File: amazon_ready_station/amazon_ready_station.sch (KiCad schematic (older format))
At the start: 25 parts, among them J1 ESP 32 Left VIN GND to VP EN, J2 IR_RECVR_GND_VIN_DAT, J5 ESP32 Right 3V3 GND to D22 D23, J7 BRKOUT_LEFT, J8 BRKOUT_RIGHT, Q1 2N2219

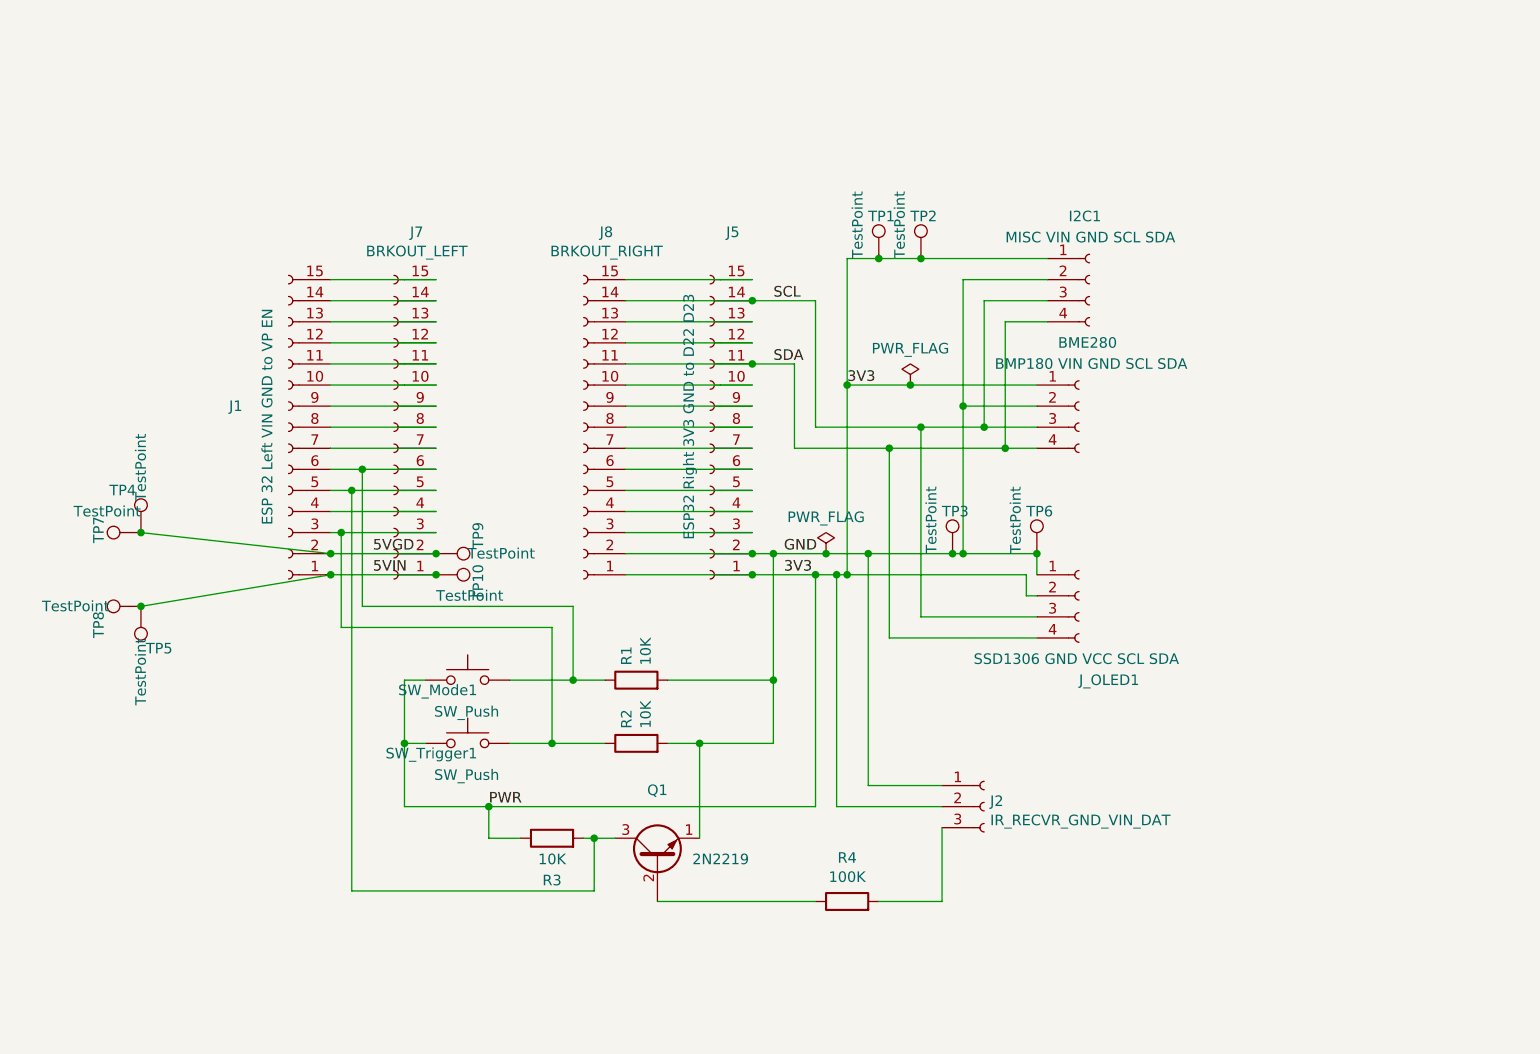
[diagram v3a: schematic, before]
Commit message: added screw holes and edited Pwr In plates
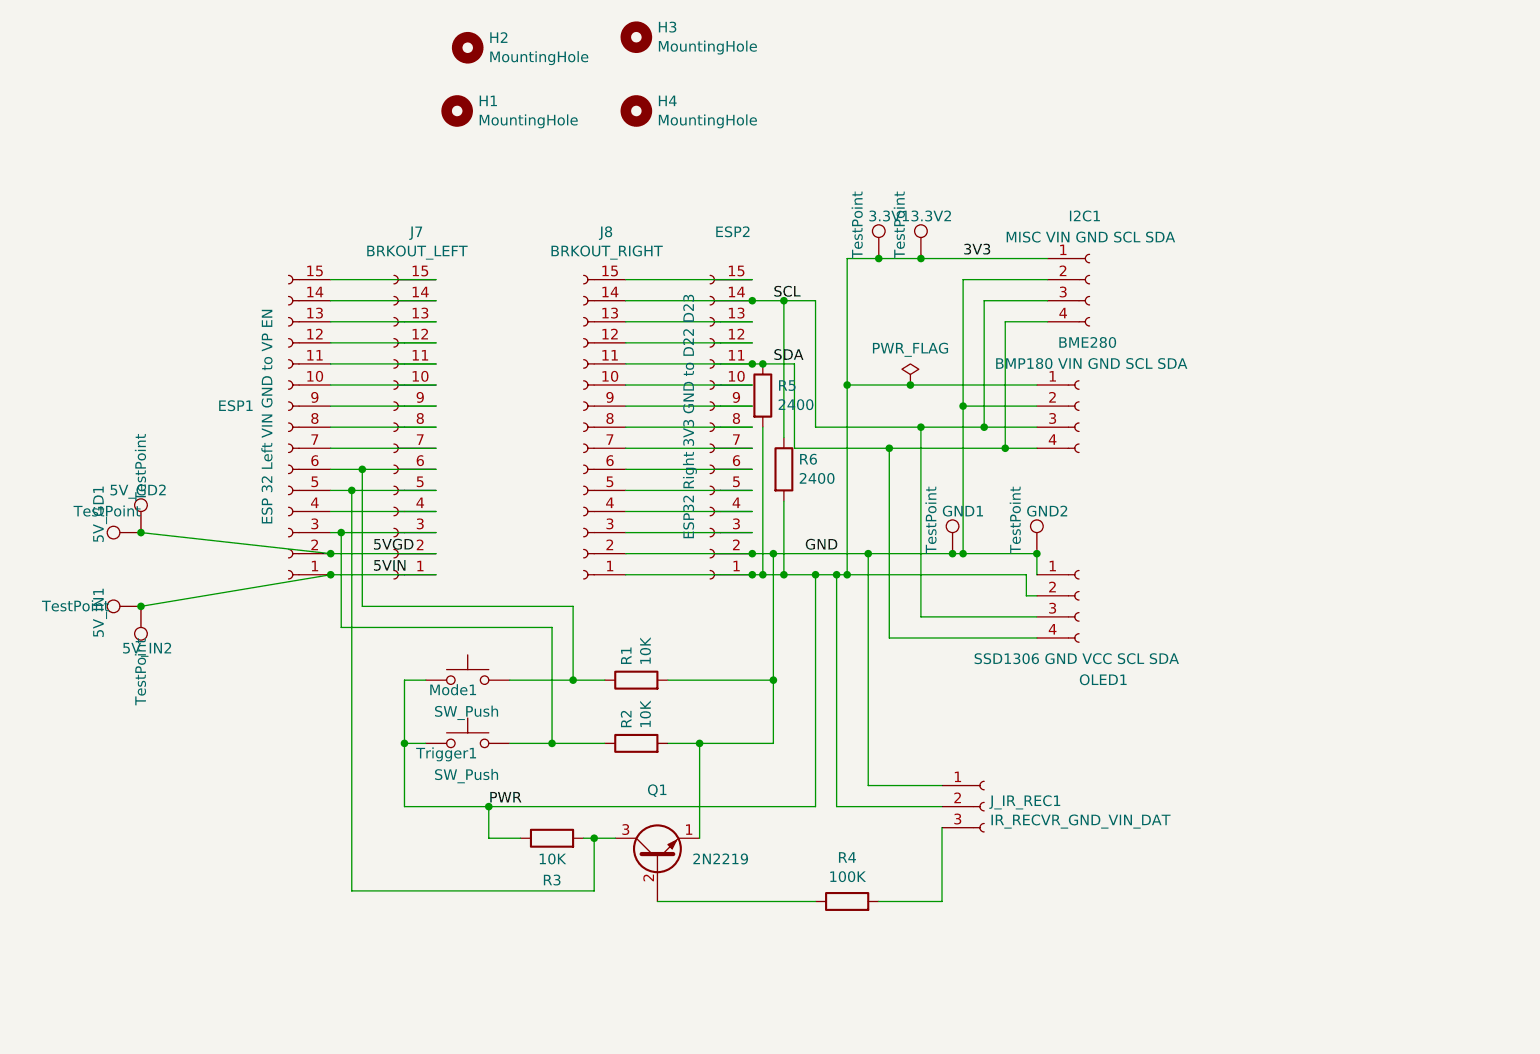
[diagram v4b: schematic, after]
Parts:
- removed TP10: TestPoint, amazon_ready_station:pad_left, symbol Connector:TestPoint
- removed TP9: TestPoint, amazon_ready_station:pad_right, symbol Connector:TestPoint
- added H1, H2, H3, H4: MountingHole, MountingHole:MountingHole_2.2mm_M2, symbol Mechanical:MountingHole
- added R5, R6: 2400, Resistor_SMD:R_0805_2012Metric_Pad1.20x1.40mm_HandSolder, symbol Device:R
- renumbered TP1 to 3.3V1, TP2 to 3.3V2, TP7 to 5V_GD1, TP4 to 5V_GD2, TP8 to 5V_IN1, TP5 to 5V_IN2, J1 to ESP1, J5 to ESP2, TP3 to GND1, TP6 to GND2, J2 to J_IR_REC1, SW_Mode1 to Mode1, J_OLED1 to OLED1, SW_Trigger1 to Trigger1
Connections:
- net 3V3: now also R5.2, R6.2
- net SCL: now also R6.1
- net SDA: now also R5.1
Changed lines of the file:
@@
 $EndComp
 $Comp
-L power:PWR_FLAG #FLG02
-U 1 1 604AC76B
-P 4700 4750
-F 0 "#FLG02" H 4700 4825 50  0001 C CNN
-F 1 "PWR_FLAG" H 4700 4923 50  0000 C CNN
-F 2 "" H 4700 4750 50  0001 C CNN
-F 3 "~" H 4700 4750 50  0001 C CNN
-	1    4700 4750
-	1    0    0    -1
-$EndComp
-$Comp
-L Connector:Conn_01x15_Female J1
+L Connector:Conn_01x15_Female ESP1
 U 1 1 604B94AB
 P 2150 4150
-F 0 "J1" H 2400 4050 50  0000 C CNN
+F 0 "ESP1" H 2400 4050 50  0000 C CNN
 F 1 "ESP 32 Left VIN GND to VP EN" V 2250 4100 50  0000 C CNN
 F 2 "Connector_PinSocket_2.54mm:PinSocket_1x15_P2.54mm_Vertical" H 2150 4150 50  0001 C CNN
@@
 $EndComp
 Wire Wire Line
-	4350 3850 4550 3850
-Wire Wire Line
-	4350 3550 4650 3550
+	4350 3850 4400 3850
+Wire Wire Line
+	4350 3550 4500 3550
 $Comp
 L Connector:Conn_01x04_Female BME280
@@
 $EndComp
 $Comp
-L Connector:Conn_01x04_Female J_OLED1
+L Connector:Conn_01x04_Female OLED1
 U 1 1 604E4BCE
 P 5900 4950
-F 0 "J_OLED1" H 5900 4550 50  0000 L CNN
+F 0 "OLED1" H 5900 4550 50  0000 L CNN
 F 1 "SSD1306 GND VCC SCL SDA" H 5400 4650 50  0000 L CNN
 F 2 "Connector_PinSocket_2.54mm:PinSocket_1x04_P2.54mm_Vertical" H 5900 4950 50  0001 C CNN
@@
 $EndComp
 $Comp
-L Connector:Conn_01x15_Female J5
+L Connector:Conn_01x15_Female ESP2
 U 1 1 604EB918
 P 4150 4150
-F 0 "J5" H 4042 3225 50  0000 C CNN
+F 0 "ESP2" H 4042 3225 50  0000 C CNN
 F 1 "ESP32 Right 3V3 GND to D22 D23" V 4250 4100 50  0000 C CNN
 F 2 "Connector_PinSocket_2.54mm:PinSocket_1x15_P2.54mm_Vertical" H 4150 4150 50  0001 C CNN
@@
 	-1   0    0    1
 $EndComp
-Text Label 4500 4750 0    50   ~ 0
+Text Label 4600 4750 0    50   ~ 0
 GND
 Text Label 4450 3850 0    50   ~ 0
@@
 Text Label 4450 3550 0    50   ~ 0
 SCL
-Text Label 4500 4850 0    50   ~ 0
-3V3
 Connection ~ 4450 4750
-Wire Wire Line
-	4450 4750 4700 4750
 $Comp
 L Device:R R1
@@
 $EndComp
 $Comp
-L Switch:SW_Push SW_Trigger1
+L Switch:SW_Push Trigger1
 U 1 1 604FFFBF
 P 3000 5650
-F 0 "SW_Trigger1" H 3046 5602 50  0000 R CNN
+F 0 "Trigger1" H 3046 5602 50  0000 R CNN
 F 1 "SW_Push" H 3150 5500 50  0000 R CNN
 F 2 "Button_Switch_SMD:SW_Push_1P1T_NO_6x6mm_H9.5mm" H 3000 5850 50  0001 C CNN
@@
 	4650 6400 3900 6400
 $Comp
-L Connector:Conn_01x03_Female J2
+L Connector:Conn_01x03_Female J_IR_REC1
 U 1 1 60683231
 P 5450 5950
-F 0 "J2" H 5478 5976 50  0000 L CNN
+F 0 "J_IR_REC1" H 5478 5976 50  0000 L CNN
 F 1 "IR_RECVR_GND_VIN_DAT" H 5478 5885 50  0000 L CNN
 F 2 "Connector_PinSocket_2.54mm:PinSocket_1x03_P2.54mm_Horizontal" H 5450 5950 50  0001 C CNN
@@
 Wire Wire Line
 	5550 4250 5700 4250
-Text Label 4800 3950 0    50   ~ 0
-3V3
 Wire Wire Line
 	4800 3950 4800 4850
@@
 	4450 4750 4450 5350
 Wire Wire Line
-	4350 4850 4650 4850
+	4350 4850 4400 4850
 Wire Wire Line
 	4800 3350 4800 3950
@@
 Wire Wire Line
 	5000 4250 5550 4250
-Connection ~ 4700 4750
 Wire Wire Line
 	5150 4150 5150 5050
@@
 	5150 4150 5450 4150
 $Comp
-L Connector:TestPoint TP1
+L Connector:TestPoint 3.3V1
 U 1 1 607606D6
 P 4950 3350
-F 0 "TP1" H 4900 3550 50  0000 L CNN
+F 0 "3.3V1" H 4900 3550 50  0000 L CNN
 F 1 "TestPoint" V 4850 3350 50  0000 L CNN
 F 2 "TestPoint:TestPoint_THTPad_D2.0mm_Drill1.0mm" H 5150 3350 50  0001 C CNN
@@
 Connection ~ 4950 3350
 $Comp
-L Connector:TestPoint TP2
+L Connector:TestPoint 3.3V2
 U 1 1 6076206D
 P 5150 3350
-F 0 "TP2" H 5100 3550 50  0000 L CNN
+F 0 "3.3V2" H 5100 3550 50  0000 L CNN
 F 1 "TestPoint" V 5050 3350 50  0000 L CNN
 F 2 "TestPoint:TestPoint_THTPad_D2.0mm_Drill1.0mm" H 5350 3350 50  0001 C CNN
@@
 Connection ~ 5150 3350
 $Comp
-L Connector:TestPoint TP3
+L Connector:TestPoint GND1
 U 1 1 60762F17
 P 5300 4750
-F 0 "TP3" H 5250 4950 50  0000 L CNN
+F 0 "GND1" H 5250 4950 50  0000 L CNN
 F 1 "TestPoint" V 5200 4750 50  0000 L CNN
 F 2 "TestPoint:TestPoint_THTPad_D2.0mm_Drill1.0mm" H 5500 4750 50  0001 C CNN
@@
 	5300 4750 5350 4750
 $Comp
-L Connector:TestPoint TP6
+L Connector:TestPoint GND2
 U 1 1 6076314C
 P 5700 4750
-F 0 "TP6" H 5650 4950 50  0000 L CNN
+F 0 "GND2" H 5650 4950 50  0000 L CNN
 F 1 "TestPoint" V 5600 4750 50  0000 L CNN
 F 2 "TestPoint:TestPoint_THTPad_D2.0mm_Drill1.0mm" H 5900 4750 50  0001 C CNN
@@
 Text Label 2550 4750 0    50   ~ 0
 5VGD
-Connection ~ 2850 4850
-$Comp
-L Connector:TestPoint TP10
-U 1 1 605C250F
-P 2850 4850
-F 0 "TP10" H 2800 5050 50  0000 L CNN
-F 1 "TestPoint" V 2950 4850 50  0000 L CNN
-F 2 "amazon_ready_station:pad_left" H 3050 4850 50  0001 C CNN
-F 3 "~" H 3050 4850 50  0001 C CNN
-	1    2850 4850
-	0    1    1    0
-$EndComp
-$Comp
-L Connector:TestPoint TP9
-U 1 1 605C4012
-P 2850 4750
-F 0 "TP9" H 2700 4950 50  0000 L CNN
-F 1 "TestPoint" V 2850 4900 50  0000 L CNN
-F 2 "amazon_ready_station:pad_right" H 3050 4750 50  0001 C CNN
-F 3 "~" H 3050 4750 50  0001 C CNN
-	1    2850 4750
-	0    1    1    0
-$EndComp
-Connection ~ 2850 4750
 Wire Wire Line
 	2350 4750 1450 4650
@@
 Connection ~ 2350 4850
 $Comp
-L Connector:TestPoint TP8
+L Connector:TestPoint 5V_IN1
 U 1 1 605CDAFA
 P 1450 5000
-F 0 "TP8" H 1300 5200 50  0000 L CNN
+F 0 "5V_IN1" H 1300 5200 50  0000 L CNN
 F 1 "TestPoint" V 1450 5150 50  0000 L CNN
 F 2 "TestPoint:TestPoint_THTPad_D2.0mm_Drill1.0mm" H 1650 5000 50  0001 C CNN
@@
 $EndComp
 $Comp
-L Connector:TestPoint TP7
+L Connector:TestPoint 5V_GD1
 U 1 1 605CE0C4
 P 1450 4650
-F 0 "TP7" H 1400 4850 50  0000 L CNN
+F 0 "5V_GD1" H 1400 4850 50  0000 L CNN
 F 1 "TestPoint" V 1550 4650 50  0000 L CNN
 F 2 "TestPoint:TestPoint_THTPad_D2.0mm_Drill1.0mm" H 1650 4650 50  0001 C CNN
@@
 $EndComp
 Wire Wire Line
-	4700 4750 4900 4750
-Wire Wire Line
 	4900 4750 4900 5850
 Wire Wire Line
@@
 	5350 4750 5700 4750
 $Comp
-L Switch:SW_Push SW_Mode1
+L Switch:SW_Push Mode1
 U 1 1 6063A1F9
 P 3000 5350
-F 0 "SW_Mode1" H 3046 5302 50  0000 R CNN
+F 0 "Mode1" H 3046 5302 50  0000 R CNN
 F 1 "SW_Push" H 3150 5200 50  0000 R CNN
 F 2 "Button_Switch_SMD:SW_Push_1P1T_NO_6x6mm_H9.5mm" H 3000 5550 50  0001 C CNN
@@
 	2800 5350 2700 5350
 $Comp
-L Connector:TestPoint TP5
+L Connector:TestPoint 5V_IN2
 U 1 1 60657975
 P 1450 5000
-F 0 "TP5" H 1300 5200 50  0000 L CNN
+F 0 "5V_IN2" H 1300 5200 50  0000 L CNN
 F 1 "TestPoint" V 1450 5150 50  0000 L CNN
 F 2 "TestPoint:TestPoint_THTPad_D2.0mm_Drill1.0mm" H 1650 5000 50  0001 C CNN
@@
 Connection ~ 1450 5000
 $Comp
-L Connector:TestPoint TP4
+L Connector:TestPoint 5V_GD2
 U 1 1 60658198
 P 1450 4650
-F 0 "TP4" H 1300 4850 50  0000 L CNN
+F 0 "5V_GD2" H 1300 4850 50  0000 L CNN
 F 1 "TestPoint" V 1450 4800 50  0000 L CNN
 F 2 "TestPoint:TestPoint_THTPad_D2.0mm_Drill1.0mm" H 1650 4650 50  0001 C CNN
@@
 $EndComp
 Connection ~ 1450 4650
+$Comp
+L Device:R R5
+U 1 1 605D37E2
+P 4400 4000
+F 0 "R5" H 4470 4046 50  0000 L CNN
+F 1 "2400" H 4470 3955 50  0000 L CNN
+F 2 "Resistor_SMD:R_0805_2012Metric_Pad1.20x1.40mm_HandSolder" V 4330 4000 50  0001 C CNN
+F 3 "~" H 4400 4000 50  0001 C CNN
+	1    4400 4000
+	1    0    0    -1
+$EndComp
+Connection ~ 4400 3850
+Wire Wire Line
+	4400 3850 4550 3850
+Wire Wire Line
+	4400 4150 4400 4850
+Connection ~ 4400 4850
+Wire Wire Line
+	4400 4850 4500 4850
+$Comp
+L Device:R R6
+U 1 1 605D9489
+P 4500 4350
+F 0 "R6" H 4570 4396 50  0000 L CNN
+F 1 "2400" H 4570 4305 50  0000 L CNN
+F 2 "Resistor_SMD:R_0805_2012Metric_Pad1.20x1.40mm_HandSolder" V 4430 4350 50  0001 C CNN
+F 3 "~" H 4500 4350 50  0001 C CNN
+	1    4500 4350
+	1    0    0    -1
+$EndComp
+Wire Wire Line
+	4500 3550 4500 4200
+Connection ~ 4500 3550
+Wire Wire Line
+	4500 3550 4650 3550
+Connection ~ 4500 4850
+Wire Wire Line
+	4500 4850 4650 4850
+Wire Wire Line
+	4500 4500 4500 4850
+$Comp
+L Mechanical:MountingHole H2
+U 1 1 6062E33E
+P 3000 2350
+F 0 "H2" H 3100 2396 50  0000 L CNN
+F 1 "MountingHole" H 3100 2305 50  0000 L CNN
+F 2 "MountingHole:MountingHole_2.2mm_M2" H 3000 2350 50  0001 C CNN
+F 3 "~" H 3000 2350 50  0001 C CNN
+	1    3000 2350
+	1    0    0    -1
+$EndComp
+$Comp
+L Mechanical:MountingHole H3
+U 1 1 6062E7A6
+P 3800 2300
+F 0 "H3" H 3900 2346 50  0000 L CNN
+F 1 "MountingHole" H 3900 2255 50  0000 L CNN
+F 2 "MountingHole:MountingHole_2.2mm_M2" H 3800 2300 50  0001 C CNN
+F 3 "~" H 3800 2300 50  0001 C CNN
+	1    3800 2300
+	1    0    0    -1
+$EndComp
+$Comp
+L Mechanical:MountingHole H4
+U 1 1 6062E97D
+P 3800 2650
+F 0 "H4" H 3900 2696 50  0000 L CNN
+F 1 "MountingHole" H 3900 2605 50  0000 L CNN
+F 2 "MountingHole:MountingHole_2.2mm_M2" H 3800 2650 50  0001 C CNN
+F 3 "~" H 3800 2650 50  0001 C CNN
+	1    3800 2650
+	1    0    0    -1
+$EndComp
+$Comp
+L Mechanical:MountingHole H1
+U 1 1 6062EB1C
+P 2950 2650
+F 0 "H1" H 3050 2696 50  0000 L CNN
+F 1 "MountingHole" H 3050 2605 50  0000 L CNN
+F 2 "MountingHole:MountingHole_2.2mm_M2" H 2950 2650 50  0001 C CNN
+F 3 "~" H 2950 2650 50  0001 C CNN
+	1    2950 2650
+	1    0    0    -1
+$EndComp
+Wire Wire Line
+	4450 4750 4900 4750
+Text Label 5350 3350 0    50   ~ 0
+3V3
 $EndSCHEMATC
